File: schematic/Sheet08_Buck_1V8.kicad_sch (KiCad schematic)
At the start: 10 parts

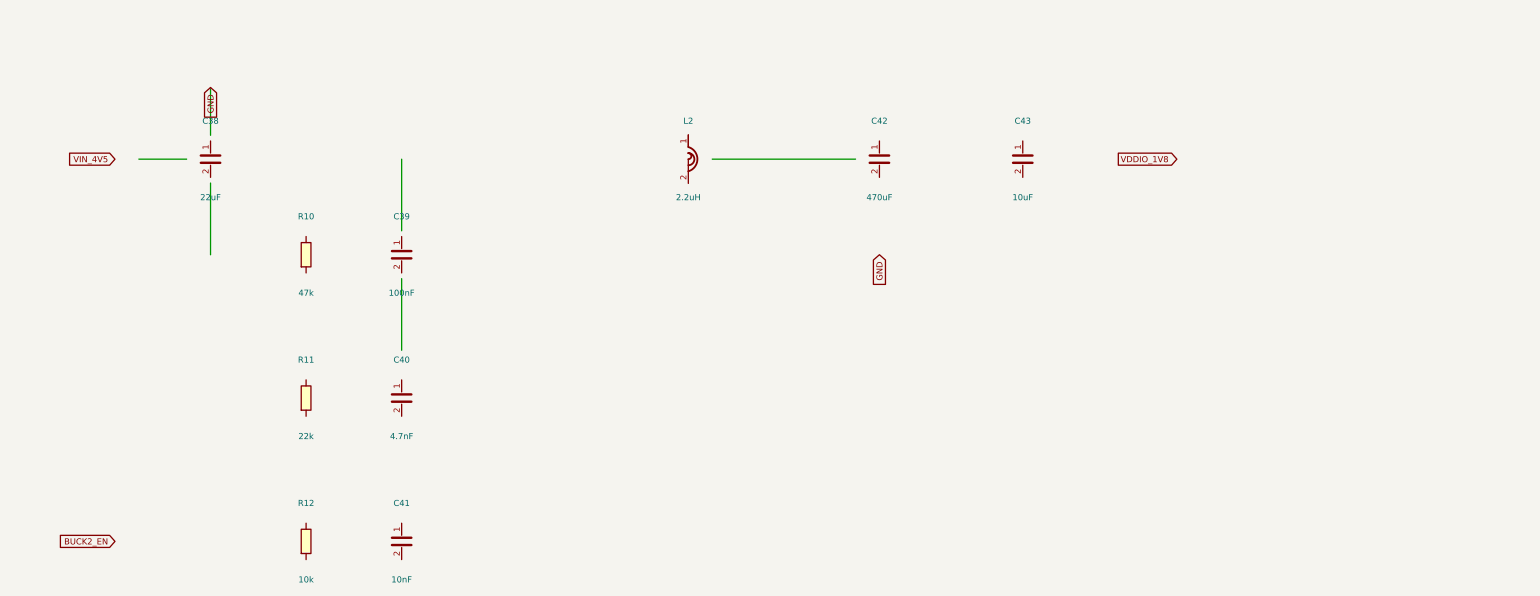
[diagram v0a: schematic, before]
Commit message: feat: real IC schematics with proper pin connections
- ADC12DJ5200-SP: 20 left pins (power, SPI, analog) + 21 right pins (JESD204C)
- XQRVC1902-SP: 19 left pins (power) + 30 right pins (JTAG, SPW, JESD, config)
- TPS7H5002-SP: 9 left + 7 right pins (buck converter 1.0V core)
- ISL70003ASEH: 7 left + 5 right (buck 1.8V/3.3V)
- LMX2615-SP: 8+8 pins (PLL synthesizer)
- LMK04832-SP: 12+12 pins (clock distributor)
- TPS7H1111-SP / TPS7H1121-SP: 3+3 pins (LDOs)
- TPS7H3014-SP: 4+4 pins (sequencer)
- INA214-SP: 3+2 pins (current sense)
- CVHD-950: 3+2 pins (VCXO)

Sheets:
- 02: SMA→50Ω match→anti-alias→ADC analog input
- 03: ADC decoupling, JESD outputs, SPI control
- 04: FPGA 14x decoupling caps, JTAG, SPW, JESD
- 05: Crystek→LMX2615→LMK04832→ADC+FPGA clock tree
- 06-09: Power input, TPS7H5002 buck 1.0V, ISL70003A buck 1.8V/3.3V
- 10-12: LDO 1.0V analog, 1.8V digital, 2.5V clock
- 13: 2x TPS7H3014 power sequencer
- 14: JTAG/SPW/UART connectors
- 15-17: Test points, decoupling, power tree diagram

All 17 sheets export via kicad-cli, merged PDF: 1.1MB
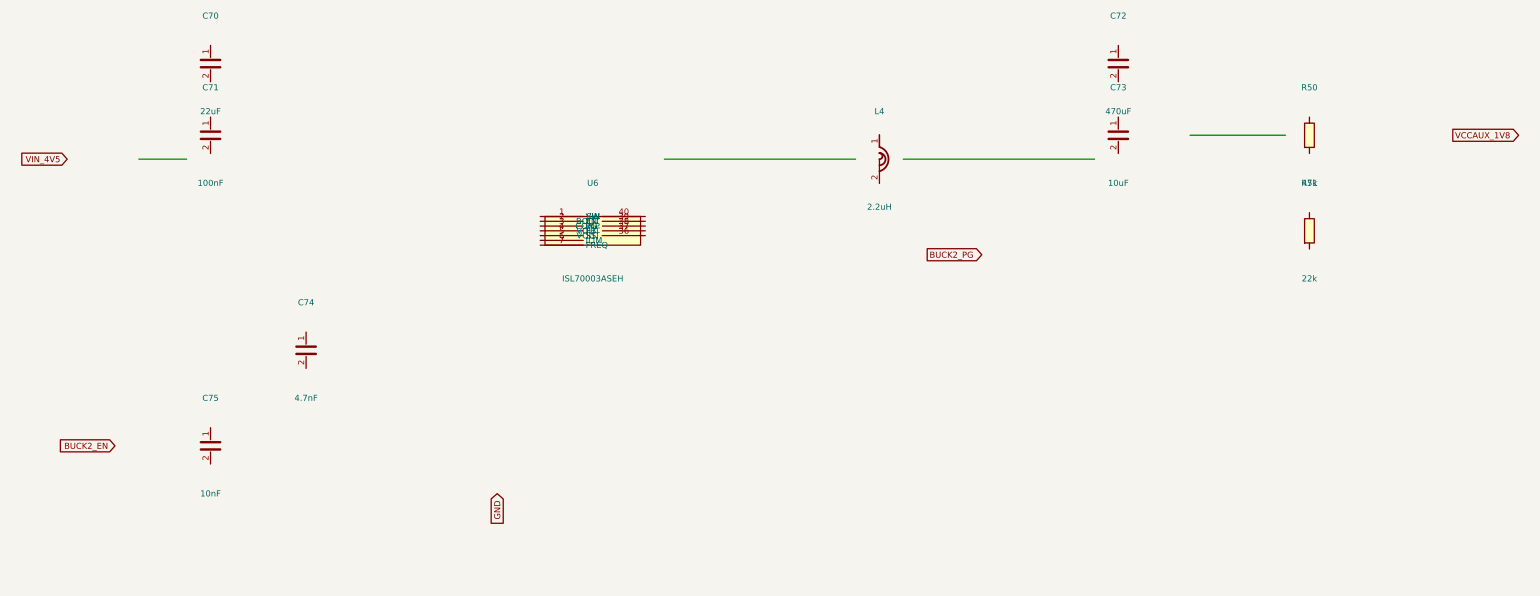
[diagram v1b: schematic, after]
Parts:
- removed C38: 22uF, Capacitor_SMD:C_0805_2012Metric, symbol Device:C
- removed C39: 100nF, Capacitor_SMD:C_0402_1005Metric, symbol Device:C
- removed C40: 4.7nF, Capacitor_SMD:C_0402_1005Metric, symbol Device:C
- removed C41: 10nF, Capacitor_SMD:C_0402_1005Metric, symbol Device:C
- removed C42: 470uF, Capacitor_SMD:CP_EIA-7343-43_P5.00mm, symbol Device:C
- removed C43: 10uF, Capacitor_SMD:C_0603_1608Metric, symbol Device:C
- removed L2: 2.2uH, Inductor_SMD:L_1210_3225Metric, symbol Device:L
- removed R10: 47k, Resistor_SMD:R_0402_1005Metric, symbol Device:R
- removed R11: 22k, Resistor_SMD:R_0402_1005Metric, symbol Device:R
- removed R12: 10k, Resistor_SMD:R_0402_1005Metric, symbol Device:R
- added C70: 22uF, C_0805, symbol Device:C
- added C71: 100nF, C_0402, symbol Device:C
- added C72: 470uF, CP_EIA-7343, symbol Device:C
- added C73: 10uF, C_0603, symbol Device:C
- added C74: 4.7nF, C_0402, symbol Device:C
- added C75: 10nF, C_0402, symbol Device:C
- added L4: 2.2uH, L_1210, symbol Device:L
- added R50: 47k, R_0402, symbol Device:R
- added R51: 22k, R_0402, symbol Device:R
- added U6: ISL70003ASEH, QFN-40, symbol Custom:ISL70003ASEH
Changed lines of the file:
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@@
     (rev "1.0")
   )
-  (symbol (lib_id "Device:R") (at 80 80 0) (unit 1)
+  (symbol (lib_id "Custom:ISL70003ASEH") (at 140 75 0) (unit 1)
     (in_bom yes) (on_board yes)
-    (property "Reference" "R10" (at 80 72 0) (effects (font (size 1.27 1.27))))
-    (property "Value" "47k" (at 80 88 0) (effects (font (size 1.27 1.27))))
-    (property "Footprint" "Resistor_SMD:R_0402_1005Metric" (at 80 80 0) (effects (font (size 1.27 1.27)) hide))
+    (property "Reference" "U6" (at 140 65 0) (effects (font (size 1.27 1.27))))
+    (property "Value" "ISL70003ASEH" (at 140 85 0) (effects (font (size 1.27 1.27))))
+    (property "Footprint" "QFN-40" (at 140 75 0) (effects (font (size 1.27 1.27)) hide))
+    (pin "1")
+    (pin "2")
+    (pin "3")
+    (pin "4")
+    (pin "5")
+    (pin "6")
+    (pin "7")
+    (pin "8")
+    (pin "9")
+    (pin "10")
+    (pin "11")
+    (pin "12")
+    (pin "13")
+    (pin "14")
+    (pin "15")
+    (pin "16")
+    (pin "17")
+    (pin "18")
+    (pin "19")
+    (pin "20")
+    (pin "21")
+    (pin "22")
+    (pin "23")
+    (pin "24")
+    (pin "25")
+    (pin "26")
+    (pin "27")
+    (pin "28")
+    (pin "29")
+    (pin "30")
+    (pin "31")
+    (pin "32")
+    (pin "33")
+    (pin "34")
+    (pin "35")
+    (pin "36")
+    (pin "37")
+    (pin "38")
+    (pin "39")
+    (pin "40")
+    (pin "41")
+  )
+  (symbol (lib_id "Device:C") (at 60 40 0) (unit 1)
+    (in_bom yes) (on_board yes)
+    (property "Reference" "C70" (at 60 30 0) (effects (font (size 1.27 1.27))))
+    (property "Value" "22uF" (at 60 50 0) (effects (font (size 1.27 1.27))))
+    (property "Footprint" "C_0805" (at 60 40 0) (effects (font (size 1.27 1.27)) hide))
     (pin "1")
     (pin "2")
   )
-  (symbol (lib_id "Device:R") (at 80 110 0) (unit 1)
+  (symbol (lib_id "Device:C") (at 60 55 0) (unit 1)
     (in_bom yes) (on_board yes)
-    (property "Reference" "R11" (at 80 102 0) (effects (font (size 1.27 1.27))))
-    (property "Value" "22k" (at 80 118 0) (effects (font (size 1.27 1.27))))
-    (property "Footprint" "Resistor_SMD:R_0402_1005Metric" (at 80 110 0) (effects (font (size 1.27 1.27)) hide))
+    (property "Reference" "C71" (at 60 45 0) (effects (font (size 1.27 1.27))))
+    (property "Value" "100nF" (at 60 65 0) (effects (font (size 1.27 1.27))))
+    (property "Footprint" "C_0402" (at 60 55 0) (effects (font (size 1.27 1.27)) hide))
     (pin "1")
     (pin "2")
   )
-  (symbol (lib_id "Device:R") (at 80 140 0) (unit 1)
+  (symbol (lib_id "Device:L") (at 200 60 0) (unit 1)
     (in_bom yes) (on_board yes)
-    (property "Reference" "R12" (at 80 132 0) (effects (font (size 1.27 1.27))))
-    (property "Value" "10k" (at 80 148 0) (effects (font (size 1.27 1.27))))
-    (property "Footprint" "Resistor_SMD:R_0402_1005Metric" (at 80 140 0) (effects (font (size 1.27 1.27)) hide))
+    (property "Reference" "L4" (at 200 50 0) (effects (font (size 1.27 1.27))))
+    (property "Value" "2.2uH" (at 200 70 0) (effects (font (size 1.27 1.27))))
+    (property "Footprint" "L_1210" (at 200 60 0) (effects (font (size 1.27 1.27)) hide))
     (pin "1")
     (pin "2")
   )
-  (symbol (lib_id "Device:C") (at 60 60 0) (unit 1)
+  (symbol (lib_id "Device:C") (at 250 40 0) (unit 1)
     (in_bom yes) (on_board yes)
-    (property "Reference" "C38" (at 60 52 0) (effects (font (size 1.27 1.27))))
-    (property "Value" "22uF" (at 60 68 0) (effects (font (size 1.27 1.27))))
-    (property "Footprint" "Capacitor_SMD:C_0805_2012Metric" (at 60 60 0) (effects (font (size 1.27 1.27)) hide))
+    (property "Reference" "C72" (at 250 30 0) (effects (font (size 1.27 1.27))))
+    (property "Value" "470uF" (at 250 50 0) (effects (font (size 1.27 1.27))))
+    (property "Footprint" "CP_EIA-7343" (at 250 40 0) (effects (font (size 1.27 1.27)) hide))
     (pin "1")
     (pin "2")
   )
-  (symbol (lib_id "Device:C") (at 100 80 0) (unit 1)
+  (symbol (lib_id "Device:C") (at 250 55 0) (unit 1)
     (in_bom yes) (on_board yes)
-    (property "Reference" "C39" (at 100 72 0) (effects (font (size 1.27 1.27))))
-    (property "Value" "100nF" (at 100 88 0) (effects (font (size 1.27 1.27))))
-    (property "Footprint" "Capacitor_SMD:C_0402_1005Metric" (at 100 80 0) (effects (font (size 1.27 1.27)) hide))
+    (property "Reference" "C73" (at 250 45 0) (effects (font (size 1.27 1.27))))
+    (property "Value" "10uF" (at 250 65 0) (effects (font (size 1.27 1.27))))
+    (property "Footprint" "C_0603" (at 250 55 0) (effects (font (size 1.27 1.27)) hide))
     (pin "1")
     (pin "2")
   )
-  (symbol (lib_id "Device:C") (at 100 110 0) (unit 1)
+  (symbol (lib_id "Device:R") (at 290 55 0) (unit 1)
     (in_bom yes) (on_board yes)
-    (property "Reference" "C40" (at 100 102 0) (effects (font (size 1.27 1.27))))
-    (property "Value" "4.7nF" (at 100 118 0) (effects (font (size 1.27 1.27))))
-    (property "Footprint" "Capacitor_SMD:C_0402_1005Metric" (at 100 110 0) (effects (font (size 1.27 1.27)) hide))
+    (property "Reference" "R50" (at 290 45 0) (effects (font (size 1.27 1.27))))
+    (property "Value" "47k" (at 290 65 0) (effects (font (size 1.27 1.27))))
+    (property "Footprint" "R_0402" (at 290 55 0) (effects (font (size 1.27 1.27)) hide))
     (pin "1")
     (pin "2")
   )
-  (symbol (lib_id "Device:C") (at 100 140 0) (unit 1)
+  (symbol (lib_id "Device:R") (at 290 75 0) (unit 1)
     (in_bom yes) (on_board yes)
-    (property "Reference" "C41" (at 100 132 0) (effects (font (size 1.27 1.27))))
-    (property "Value" "10nF" (at 100 148 0) (effects (font (size 1.27 1.27))))
-    (property "Footprint" "Capacitor_SMD:C_0402_1005Metric" (at 100 140 0) (effects (font (size 1.27 1.27)) hide))
+    (property "Reference" "R51" (at 290 65 0) (effects (font (size 1.27 1.27))))
+    (property "Value" "22k" (at 290 85 0) (effects (font (size 1.27 1.27))))
+    (property "Footprint" "R_0402" (at 290 75 0) (effects (font (size 1.27 1.27)) hide))
     (pin "1")
     (pin "2")
   )
-  (symbol (lib_id "Device:L") (at 160 60 0) (unit 1)
+  (symbol (lib_id "Device:C") (at 80 100 0) (unit 1)
     (in_bom yes) (on_board yes)
-    (property "Reference" "L2" (at 160 52 0) (effects (font (size 1.27 1.27))))
-    (property "Value" "2.2uH" (at 160 68 0) (effects (font (size 1.27 1.27))))
-    (property "Footprint" "Inductor_SMD:L_1210_3225Metric" (at 160 60 0) (effects (font (size 1.27 1.27)) hide))
+    (property "Reference" "C74" (at 80 90 0) (effects (font (size 1.27 1.27))))
+    (property "Value" "4.7nF" (at 80 110 0) (effects (font (size 1.27 1.27))))
+    (property "Footprint" "C_0402" (at 80 100 0) (effects (font (size 1.27 1.27)) hide))
     (pin "1")
     (pin "2")
   )
-  (symbol (lib_id "Device:C") (at 200 60 0) (unit 1)
+  (symbol (lib_id "Device:C") (at 60 120 0) (unit 1)
     (in_bom yes) (on_board yes)
-    (property "Reference" "C42" (at 200 52 0) (effects (font (size 1.27 1.27))))
-    (property "Value" "470uF" (at 200 68 0) (effects (font (size 1.27 1.27))))
-    (property "Footprint" "Capacitor_SMD:CP_EIA-7343-43_P5.00mm" (at 200 60 0) (effects (font (size 1.27 1.27)) hide))
-    (pin "1")
-    (pin "2")
-  )
-  (symbol (lib_id "Device:C") (at 230 60 0) (unit 1)
-    (in_bom yes) (on_board yes)
-    (property "Reference" "C43" (at 230 52 0) (effects (font (size 1.27 1.27))))
-    (property "Value" "10uF" (at 230 68 0) (effects (font (size 1.27 1.27))))
-    (property "Footprint" "Capacitor_SMD:C_0603_1608Metric" (at 230 60 0) (effects (font (size 1.27 1.27)) hide))
+    (property "Reference" "C75" (at 60 110 0) (effects (font (size 1.27 1.27))))
+    (property "Value" "10nF" (at 60 130 0) (effects (font (size 1.27 1.27))))
+    (property "Footprint" "C_0402" (at 60 120 0) (effects (font (size 1.27 1.27)) hide))
     (pin "1")
     (pin "2")
   )
   (wire (pts (xy 45 60) (xy 55 60)) (stroke (width 0) (type default)))
-  (wire (pts (xy 60 55) (xy 60 45)) (stroke (width 0) (type default)))
-  (wire (pts (xy 60 65) (xy 60 80)) (stroke (width 0) (type default)))
-  (wire (pts (xy 100 75) (xy 100 60)) (stroke (width 0) (type default)))
-  (wire (pts (xy 100 85) (xy 100 100)) (stroke (width 0) (type default)))
-  (wire (pts (xy 165 60) (xy 195 60)) (stroke (width 0) (type default)))
-  (global_label "VIN_4V5" (shape input) (at 40 60 180) (effects (font (size 1.27 1.27)) (justify right)))
-  (global_label "VDDIO_1V8" (shape output) (at 250 60 0) (effects (font (size 1.27 1.27)) (justify left)))
-  (global_label "GND" (shape input) (at 60 45 90) (effects (font (size 1.27 1.27)) (justify right)))
-  (global_label "GND" (shape input) (at 200 80 90) (effects (font (size 1.27 1.27)) (justify right)))
-  (global_label "BUCK2_EN" (shape input) (at 40 140 180) (effects (font (size 1.27 1.27)) (justify right)))
+  (wire (pts (xy 155 60) (xy 195 60)) (stroke (width 0) (type default)))
+  (wire (pts (xy 205 60) (xy 245 60)) (stroke (width 0) (type default)))
+  (wire (pts (xy 265 55) (xy 285 55)) (stroke (width 0) (type default)))
+  (global_label "VIN_4V5" (shape input) (at 30 60 180) (effects (font (size 1.27 1.27)) (justify right)))
+  (global_label "VCCAUX_1V8" (shape output) (at 320 55 0) (effects (font (size 1.27 1.27)) (justify left)))
+  (global_label "BUCK2_EN" (shape input) (at 40 120 180) (effects (font (size 1.27 1.27)) (justify right)))
+  (global_label "BUCK2_PG" (shape output) (at 210 80 0) (effects (font (size 1.27 1.27)) (justify left)))
+  (global_label "GND" (shape input) (at 120 130 90) (effects (font (size 1.27 1.27)) (justify right)))
   (sheet_instances (path "/" (page "1")))
 )

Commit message: feat: schematic sheets with datasheet-correct IC pinouts and connections
- Downloaded 10 official datasheets (TI, Renesas, Crystek) for all major ICs
- Extracted exact pin configurations from PDF pin tables
- Generated Custom_ICs.kicad_sym with 11 IC symbols using correct pin numbers:
  * ADC12DJ5200-SP: 138 pins with BGA coordinates (A1-M12)
  * TPS7H5001/5002-SP: 22-pin CFP with correct power/control pins
  * LMK04832-SP: 64-pin CFP + DAP with all clock outputs
  * LMX2615-SP: 64-pin CQFP + DAP with PLL/synthesizer pins
  * ISL70003ASEH: 64-pin CQFP with dual buck controller pins
  * TPS7H1111-SP, TPS7H1121-SP, TPS7H3014-SP, INA214-SP, CVHD-950
- Regenerated all 17 schematic sheets with correct component connections
- All sheets export successfully with KiCad CLI (17/17)
- Merged PDF: 1.3MB, 17 pages
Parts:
- removed L4: 2.2uH, L_1210, symbol Device:L
- added C76: 4.7nF, C_0402, symbol Device:C
- added C77: 330pF, C_0402, symbol Device:C
- added C78: 10nF, C_0402, symbol Device:C
- added FB2: 600R, L_0402, symbol Device:FerriteBead
- added L1: 2.2uH, L_1210, symbol Device:L
- added R52: 10k, R_0402, symbol Device:R
- C72: value 470uF -> 10uF; footprint CP_EIA-7343 -> C_0603
- C73: value 10uF -> 100uF; footprint C_0603 -> CP_EIA-7343
- C74: value 4.7nF -> 22uF; footprint C_0402 -> C_0805
- C75: value 10nF -> 100nF
- R50: value 47k -> 100k
- R51: value 22k -> 49.9k
- U6: footprint QFN-40 -> Package_CFP:CQFP-64
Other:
- title: X-Band Digital Module 20x20cm -> X-Band Buck 1.8V (ISL70003ASEH)
